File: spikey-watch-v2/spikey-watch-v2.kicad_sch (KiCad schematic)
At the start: 56 parts, among them J1 USB_C_Receptacle_USB2.0_16P, J2 Conn_01x02_Pin, Q1 FDN340P, SW3 USER_SW, SW4 USER_SW, SW7 USER_SW, SW8 USER_SW, U1 ESP32-S3-WROOM-1, U2 USBLC6-2SC6, U3 AP2112K-3.3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

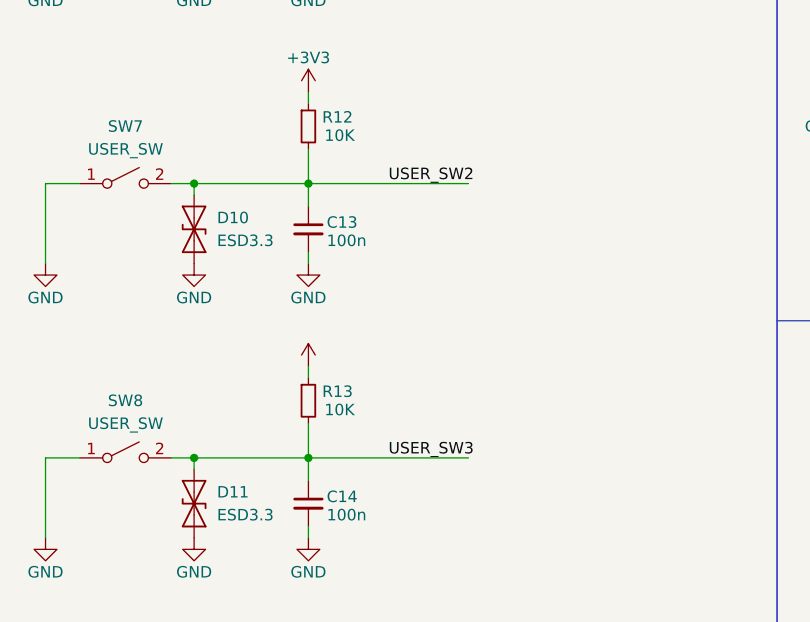
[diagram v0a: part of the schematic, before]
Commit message: improved routing
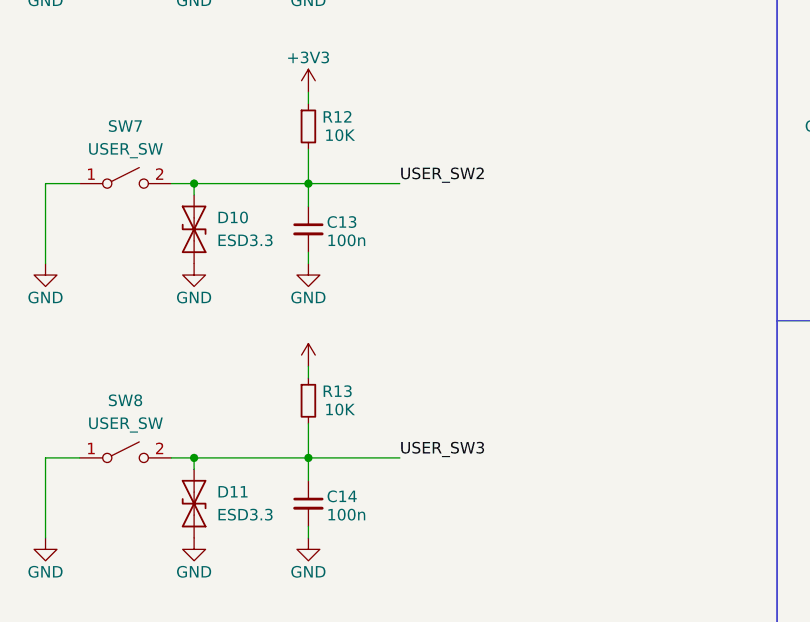
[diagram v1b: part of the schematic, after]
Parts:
- H1, H2, H3, H4: footprint MountingHole:MountingHole_2.7mm_M2.5_Pad -> MountingHole:MountingHole_3.2mm_M3
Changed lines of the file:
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@@
 	(wire
 		(pts
-			(xy 46.99 124.46) (xy 64.77 124.46)
+			(xy 46.99 124.46) (xy 57.15 124.46)
 		)
 		(stroke
@@
 	(wire
 		(pts
-			(xy 46.99 93.98) (xy 64.77 93.98)
+			(xy 46.99 93.98) (xy 57.15 93.98)
 		)
 		(stroke
@@
 	)
 	(label "USER_SW2"
-		(at 55.88 93.98 0)
+		(at 57.15 93.98 0)
 		(effects
 			(font
@@
 	)
 	(label "USER_SW3"
-		(at 55.88 124.46 0)
+		(at 57.15 124.46 0)
 		(effects
 			(font
@@
 			)
 		)
-		(property "Footprint" "MountingHole:MountingHole_2.7mm_M2.5_Pad"
+		(property "Footprint" "MountingHole:MountingHole_3.2mm_M3"
 			(at 29.21 156.21 0)
 			(hide yes)
@@
 			)
 		)
-		(property "Footprint" "MountingHole:MountingHole_2.7mm_M2.5_Pad"
+		(property "Footprint" "MountingHole:MountingHole_3.2mm_M3"
 			(at 29.21 161.29 0)
 			(hide yes)
@@
 			)
 		)
-		(property "Footprint" "MountingHole:MountingHole_2.7mm_M2.5_Pad"
+		(property "Footprint" "MountingHole:MountingHole_3.2mm_M3"
 			(at 29.21 166.37 0)
 			(hide yes)
@@
 			)
 		)
-		(property "Footprint" "MountingHole:MountingHole_2.7mm_M2.5_Pad"
+		(property "Footprint" "MountingHole:MountingHole_3.2mm_M3"
 			(at 29.21 171.45 0)
 			(hide yes)
